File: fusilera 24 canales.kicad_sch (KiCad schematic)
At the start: 28 parts, among them J1 +12V borne M6, J2 GND borne M5, U4 MCP23017-E/SO, U5 MCP23017-E/SO, U6 LM5164DDA, U7 AP2112K-3.3

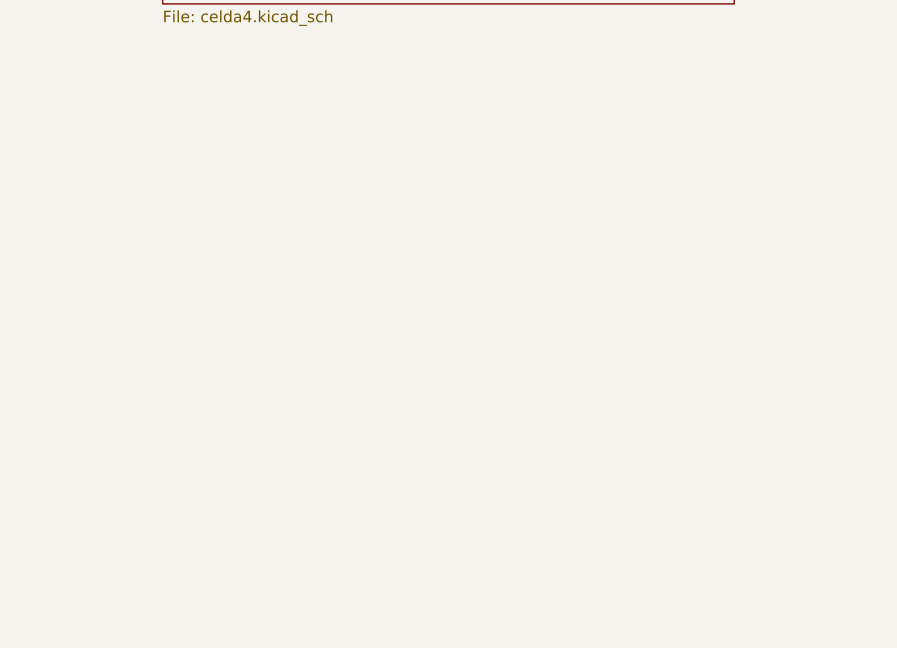
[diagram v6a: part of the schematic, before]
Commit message: Añade la Celda3, gira los canales 3 y 4 y rutea los grupos movidos de la Celda1
Agrega la tercera instancia de la celda al esquemático (referencias +200) y
pasa sus footprints al PCB. En la Celda1 los canales 3 y 4 quedan girados 180°
al lado izquierdo con la lógica compartida en el centro, y se rutean con un
enrutador de rejilla propio IS3, IS4, FALLA3, FALLA4, los umbrales y los
pull-ups de los comparadores, más las vías de plano de C18, C19, R31 y R32.
Se documenta la decisión de arquitectura y el riesgo del bus hacia el
controlador en CONTEXTO_PROYECTO.md.
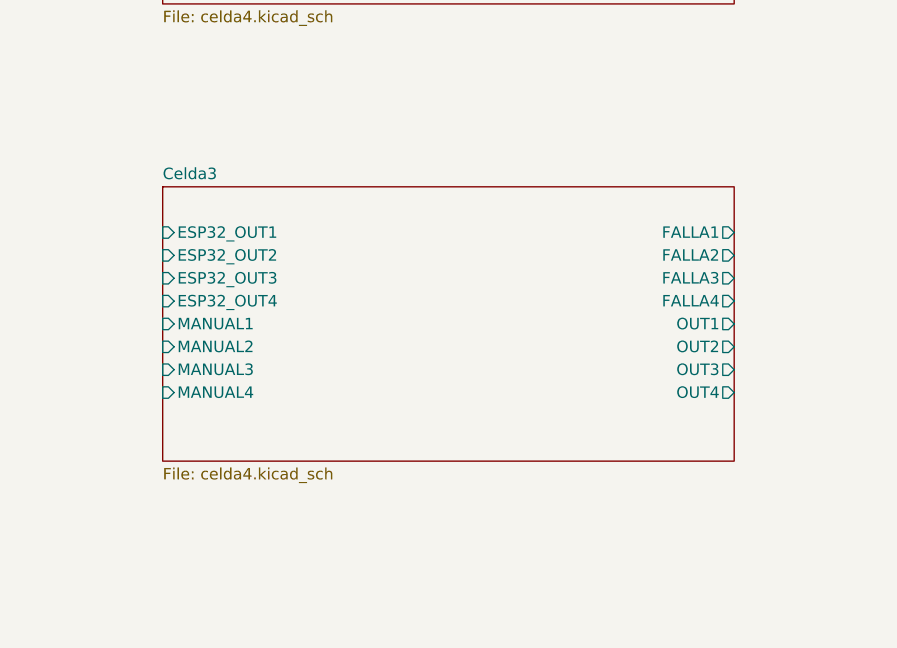
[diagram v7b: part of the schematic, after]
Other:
- added sheet Celda3 (celda4.kicad_sch)
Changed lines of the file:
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@@
+		)
+	)
+	(sheet
+		(at 88.9 292.1)
+		(size 63.5 30.48)
+		(exclude_from_sim no)
+		(in_bom yes)
+		(on_board yes)
+		(dnp no)
+		(fields_autoplaced yes)
+		(stroke
+			(width 0.1524)
+			(type solid)
+		)
+		(fill
+			(color 0 0 0 0)
+		)
+		(property "Sheetname" "Celda3"
+			(at 88.9 291.4 0)
+			(show_name no)
+			(do_not_autoplace no)
+			(effects
+				(font
+					(size 1.27 1.27)
+				)
+				(justify left bottom)
+			)
+		)
+		(property "Sheetfile" "celda4.kicad_sch"
+			(at 88.9 323.28 0)
+			(show_name no)
+			(do_not_autoplace no)
+			(effects
+				(font
+					(size 1.27 1.27)
+				)
+				(justify left top)
+			)
+		)
+		(pin "ESP32_OUT1" input
+			(at 88.9 297.18 180)
+			(effects
+				(font
+					(size 1.27 1.27)
+				)
+				(justify left)
+			)
+		)
+		(pin "ESP32_OUT2" input
+			(at 88.9 299.72 180)
+			(effects
+				(font
+					(size 1.27 1.27)
+				)
+				(justify left)
+			)
+		)
+		(pin "ESP32_OUT3" input
+			(at 88.9 302.26 180)
+			(effects
+				(font
+					(size 1.27 1.27)
+				)
+				(justify left)
+			)
+		)
+		(pin "ESP32_OUT4" input
+			(at 88.9 304.8 180)
+			(effects
+				(font
+					(size 1.27 1.27)
+				)
+				(justify left)
+			)
+		)
+		(pin "MANUAL1" input
+			(at 88.9 307.34 180)
+			(effects
+				(font
+					(size 1.27 1.27)
+				)
+				(justify left)
+			)
+		)
+		(pin "MANUAL2" input
+			(at 88.9 309.88 180)
+			(effects
+				(font
+					(size 1.27 1.27)
+				)
+				(justify left)
+			)
+		)
+		(pin "MANUAL3" input
+			(at 88.9 312.42 180)
+			(effects
+				(font
+					(size 1.27 1.27)
+				)
+				(justify left)
+			)
+		)
+		(pin "MANUAL4" input
+			(at 88.9 314.96 180)
+			(effects
+				(font
+					(size 1.27 1.27)
+				)
+				(justify left)
+			)
+		)
+		(pin "FALLA1" output
+			(at 152.4 297.18 0)
+			(effects
+				(font
+					(size 1.27 1.27)
+				)
+				(justify right)
+			)
+		)
+		(pin "FALLA2" output
+			(at 152.4 299.72 0)
+			(effects
+				(font
+					(size 1.27 1.27)
+				)
+				(justify right)
+			)
+		)
+		(pin "FALLA3" output
+			(at 152.4 302.26 0)
+			(effects
+				(font
+					(size 1.27 1.27)
+				)
+				(justify right)
+			)
+		)
+		(pin "FALLA4" output
+			(at 152.4 304.8 0)
+			(effects
+				(font
+					(size 1.27 1.27)
+				)
+				(justify right)
+			)
+		)
+		(pin "OUT1" output
+			(at 152.4 307.34 0)
+			(effects
+				(font
+					(size 1.27 1.27)
+				)
+				(justify right)
+			)
+		)
+		(pin "OUT2" output
+			(at 152.4 309.88 0)
+			(effects
+				(font
+					(size 1.27 1.27)
+				)
+				(justify right)
+			)
+		)
+		(pin "OUT3" output
+			(at 152.4 312.42 0)
+			(effects
+				(font
+					(size 1.27 1.27)
+				)
+				(justify right)
+			)
+		)
+		(pin "OUT4" output
+			(at 152.4 314.96 0)
+			(effects
+				(font
+					(size 1.27 1.27)
+				)
+				(justify right)
+			)
+		)
+		(instances
+			(project "fusilera 24 canales"
+				(path "/6451a64b-df92-4e59-b073-88385097038f"
+					(page "4")
+				)
+			)
 		)
 	)

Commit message: Conecta las celdas con el micro, dibuja el contorno y reubica los bloques
Cablea en el esquemático raíz las salidas ESP32_OUT y las entradas FALLA de las
tres celdas a pines de la ESP32 (A1) y del MCP23017 (U4) mediante etiquetas
locales, de modo que el PCB muestra el ratsnest hacia el controlador. Dibuja el
contorno de la placa en Edge.Cuts (123 x 191 mm), ajusta los planos de GND y
+3,3 V a ese contorno y reubica las celdas, el controlador y el bloque de poder.
Se registra la hoja Celda3 en el proyecto y se actualiza CONTEXTO_PROYECTO.md.
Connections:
- net D27: now reaches A1.10 (D27)
- net D14: now reaches A1.11 (D14)
- net D13: now reaches A1.13 (D13)
- net D23: now reaches A1.16 (D23)
- net VP: now reaches A1.2 (VP/GPIO36)
- net D19: now reaches A1.21 (D19)
- net D18: now reaches A1.22 (D18)
- net TX2: now reaches A1.24 (TX2/GPIO17)
- net RX2: now reaches A1.25 (RX2/GPIO16)
- net D4: now reaches A1.26 (D4)
- net VN: now reaches A1.3 (VN/GPIO39)
- net D34: now reaches A1.4 (D34)
- net D35: now reaches A1.5 (D35)
- net D32: now reaches A1.6 (D32)
- net D33: now reaches A1.7 (D33)
- net D25: now reaches A1.8 (D25)
- net D26: now reaches A1.9 (D26)
- net U4-GPA0: now reaches U4.21 (GPA0)
- net U4-GPA1: now reaches U4.22 (GPA1)
- net U4-GPA2: now reaches U4.23 (GPA2)
- net U4-GPA3: now reaches U4.24 (GPA3)
- net U4-GPA4: now reaches U4.25 (GPA4)
- net U4-GPA5: now reaches U4.26 (GPA5)
- net U4-GPA6: now reaches U4.27 (GPA6)
- net U4-GPA7: now reaches U4.28 (GPA7)
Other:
- moved on the sheet: A1, C6, U4, U5
